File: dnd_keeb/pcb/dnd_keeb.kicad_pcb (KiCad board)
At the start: 2 copper layers, 60 x 100 mm, 23 parts, among them J1 Conn_01x11, SW1 SW_DIP_x01, SW2 SW_DIP_x01, SW3 SW_DIP_x01, SW4 SW_DIP_x01, SW5 SW_DIP_x01, SW6 SW_DIP_x01, SW7 SW_DIP_x01, SW8 SW_DIP_x01, SW9 SW_DIP_x01, U1 OLED_326

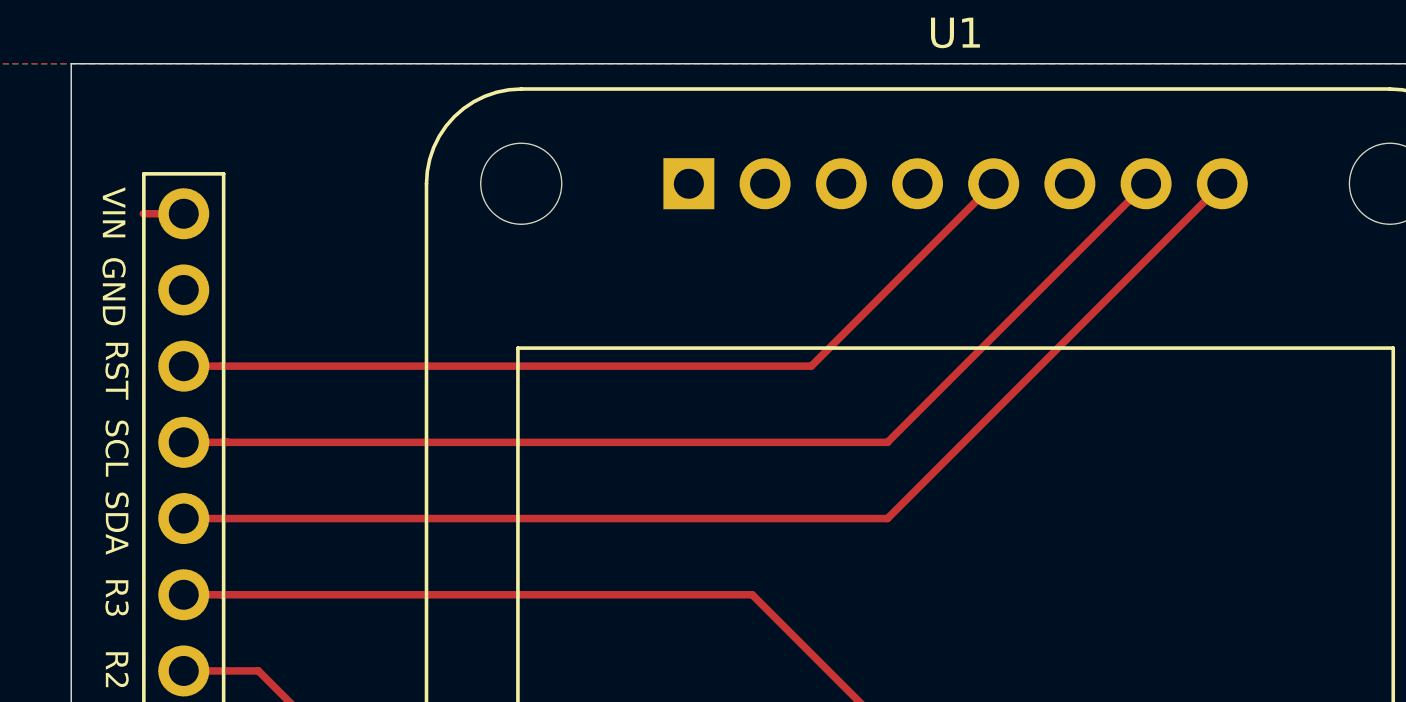
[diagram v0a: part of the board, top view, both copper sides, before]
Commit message: 🐛 [dnd_keeb] Fix pinout for OLED & update footprints + pcb
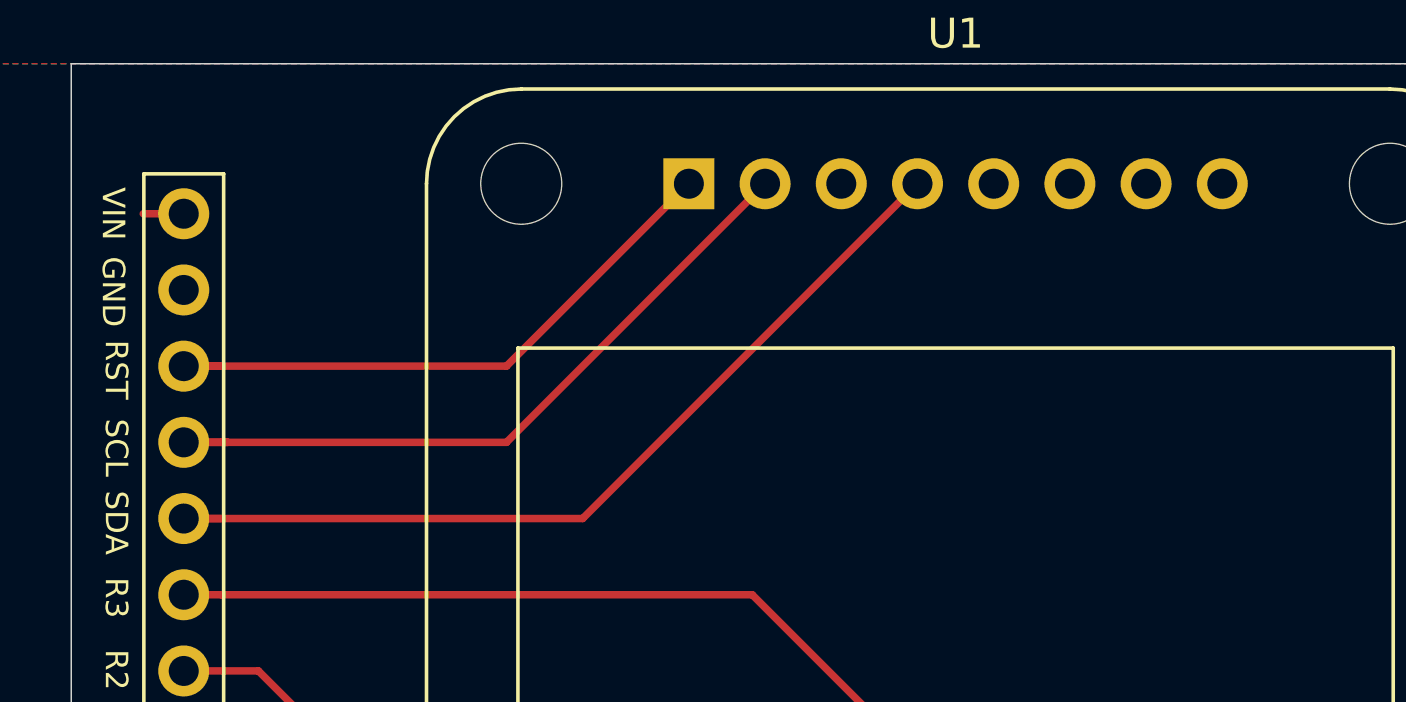
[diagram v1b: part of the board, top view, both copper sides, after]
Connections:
- J1 pad 7: SDA -> RST
- J1 pad 9: RST -> SDA
- U1 pad 1: GND -> SDA
- U1 pad 2: VIN -> SCL
- U1 pad 4: Net-(U1-Pad4) -> RST
- U1 pad 5: RST -> Net-(U1-Pad5)
- U1 pad 7: SCL -> VIN
- U1 pad 8: SDA -> GND
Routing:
- net SDA: track 39.2 -> 21.0 mm
- net SCL: track 35.9 -> 24.6 mm
- net RST: track 29.5 -> 30.3 mm

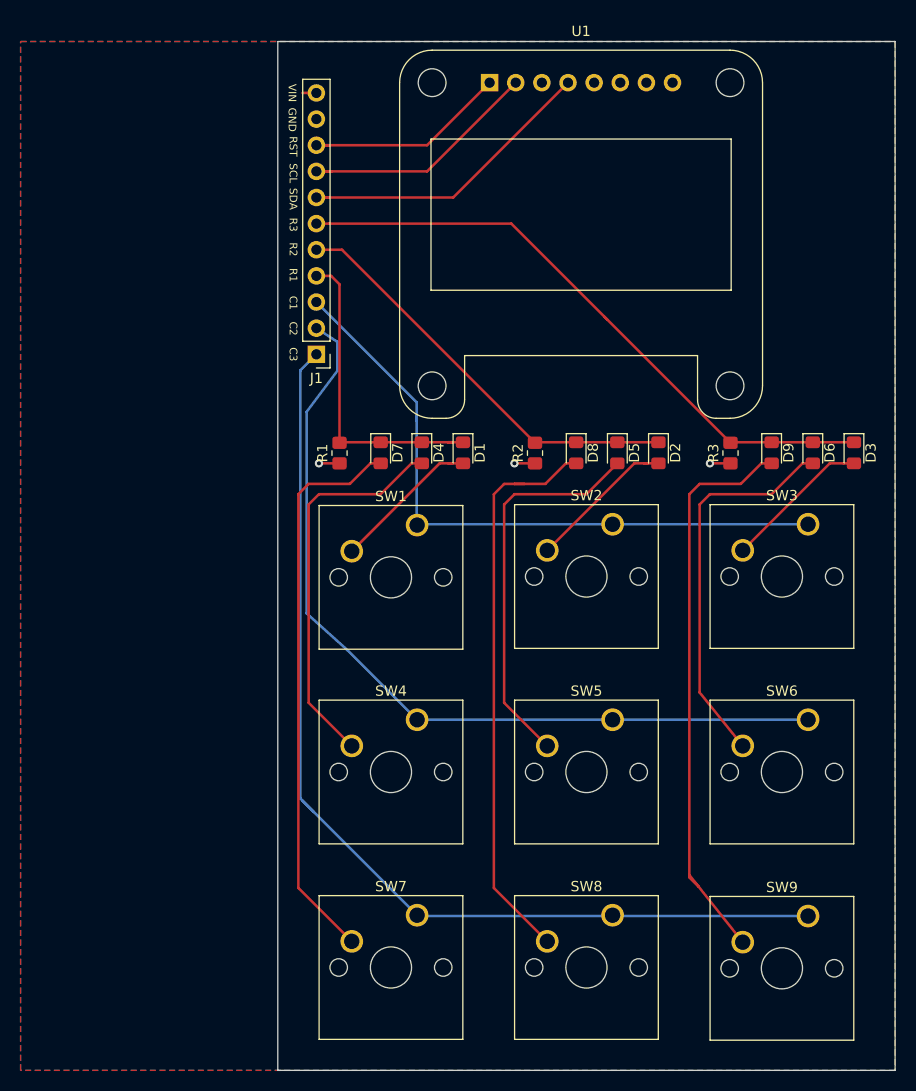
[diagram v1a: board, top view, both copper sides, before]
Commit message: ✨ [dnd_keeb] v0.2
- Added atmega4809 to board, routed row/cols + lcd to mcu
- Added ICSP + TX/RX pinout to program / debug
- Added USB micro for power
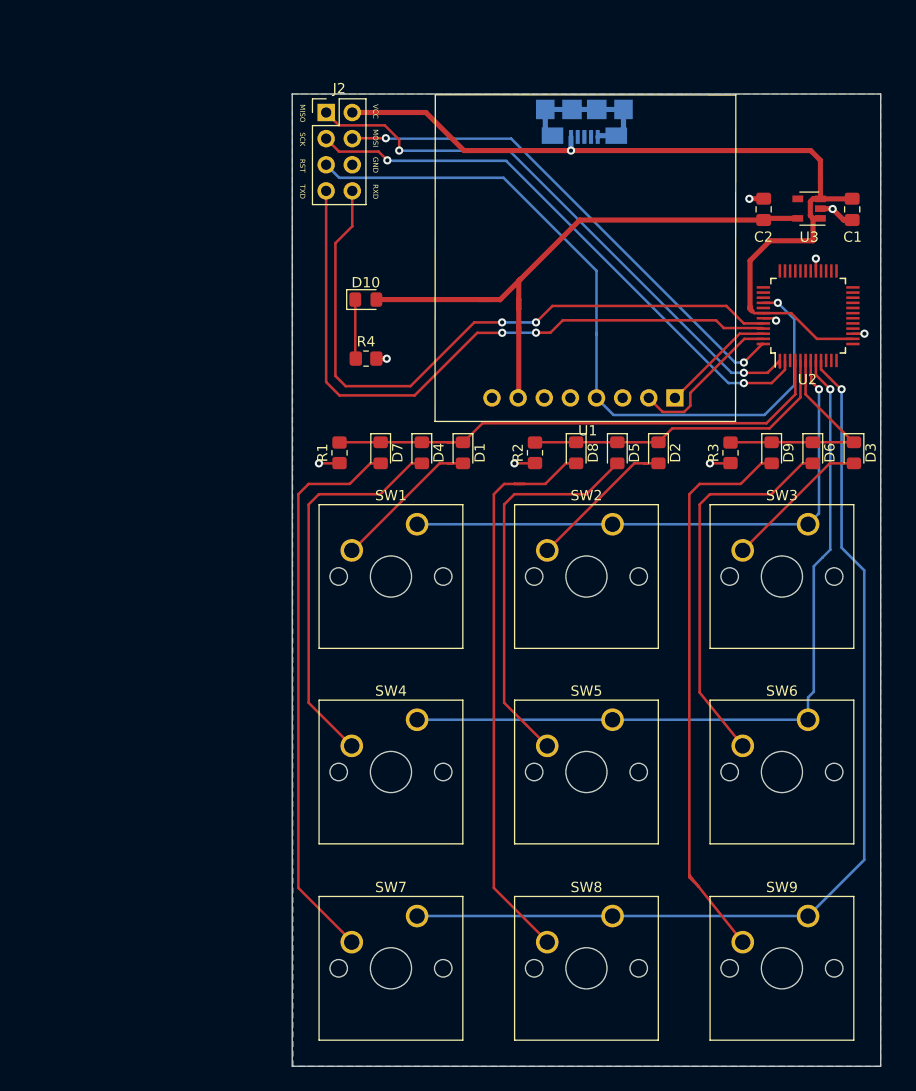
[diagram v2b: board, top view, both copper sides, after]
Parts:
- added C1: 1uF, Capacitor_SMD:C_0805_2012Metric_Pad1.18x1.45mm_HandSolder, F.Cu at (185.8, 36.3)
- added C2: 1uF, Capacitor_SMD:C_0805_2012Metric_Pad1.18x1.45mm_HandSolder, F.Cu at (177.2, 36.3)
- added D10: PWR, LED_SMD:LED_0805_2012Metric_Pad1.15x1.40mm_HandSolder, F.Cu at (138.6, 45.1)
- added J2: Conn_02x04_Odd_Even, Connector_PinHeader_2.54mm:PinHeader_2x04_P2.54mm_Vertical, F.Cu at (134.7, 26.9)
- added R4: 330, Resistor_SMD:R_0805_2012Metric_Pad1.20x1.40mm_HandSolder, F.Cu at (138.6, 50.8)
- added U2: ATmega4809-A, Package_QFP:TQFP-48_7x7mm_P0.5mm, F.Cu at (181.6, 46.6)
- added U3: AP2112K-3.3, Package_TO_SOT_SMD:SOT-23-5, F.Cu at (181.6, 36.2)
- J1: value Conn_01x11 -> USB-B Micro Receptacle 10118192-0002LF; footprint Connector_PinHeader_2.54mm:PinHeader_1x11_P2.54mm_Vertical -> dnd_keeb:AMPHENOL_10118192-0002LF; moved to B.Cu
- U1: footprint Display:Adafruit_SSD1306 -> dnd_keeb:Adafruit_326
- moved J1 33.5 mm to (159.8, 29.3), turned to 0 degrees
- moved U1 32.8 mm to (162.2, 54.7), turned to 180 degrees
- moved SW1 0.08 mm to (143.5, 66.9)
- moved SW7 0.08 mm to (143.5, 105.0)
- moved SW8 0.08 mm to (162.5, 105.0)
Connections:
- J1 pad 1: COL3 -> VCC
- J1 pad 2: COL2 -> Net-(J1-Pad2)
- J1 pad 3: COL1 -> Net-(J1-Pad3)
- J1 pad 4: ROW1 -> Net-(J1-Pad4)
- J1 pad 5: ROW2 -> GND
- U1 pad 7: VIN -> 3v3
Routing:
- net VCC: track 0.00 -> 84.1 mm, vias 0 -> 1
- net /RXD: track 0.00 -> 65.1 mm, vias 0 -> 2
- net /TXD: track 0.00 -> 64.6 mm, vias 0 -> 2
- net 3v3: track 0.00 -> 58.6 mm
- net MISO: track 0.00 -> 56.4 mm, vias 0 -> 2
- net SCK: track 0.00 -> 55.9 mm, vias 0 -> 2
- net MOSI: track 0.00 -> 50.1 mm, vias 0 -> 2
- net RST: track 30.3 -> 74.3 mm, vias 0 -> 1
- net ROW3: track 61.4 -> 21.9 mm
- net GND: track 6.00 -> 30.7 mm, vias 3 -> 9
- net ROW1: track 30.5 -> 50.0 mm
- net SDA: track 21.0 -> 11.2 mm
- net ROW2: track 41.0 -> 31.2 mm
- net COL1: track 64.2 -> 54.8 mm, vias 0 -> 1
- net SCL: track 24.6 -> 15.4 mm
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- removed copper zone on F.Cu, net VIN
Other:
- board size 60 x 100 mm -> 57.2 x 94.5 mm
- board text added: "D&D Keeb v0.2"
- board text added: "MISO"
- board text added: "MOSI"
- board text added: "RXD"
- board text added: "SCK"
- board text added: "TXD"
- board text added: "VCC"
- board text removed: "C1"
- board text removed: "C2"
- board text removed: "C3"
- board text removed: "D&D Keeb v0.1"
- board text removed: "R1"
- board text removed: "R2"
- board text removed: "R3"
- board text removed: "SCL"
- board text removed: "SDA"
- board text removed: "VIN"

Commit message: 🐛 Updating schematic so that UPDI is correctly broken out to a PIN
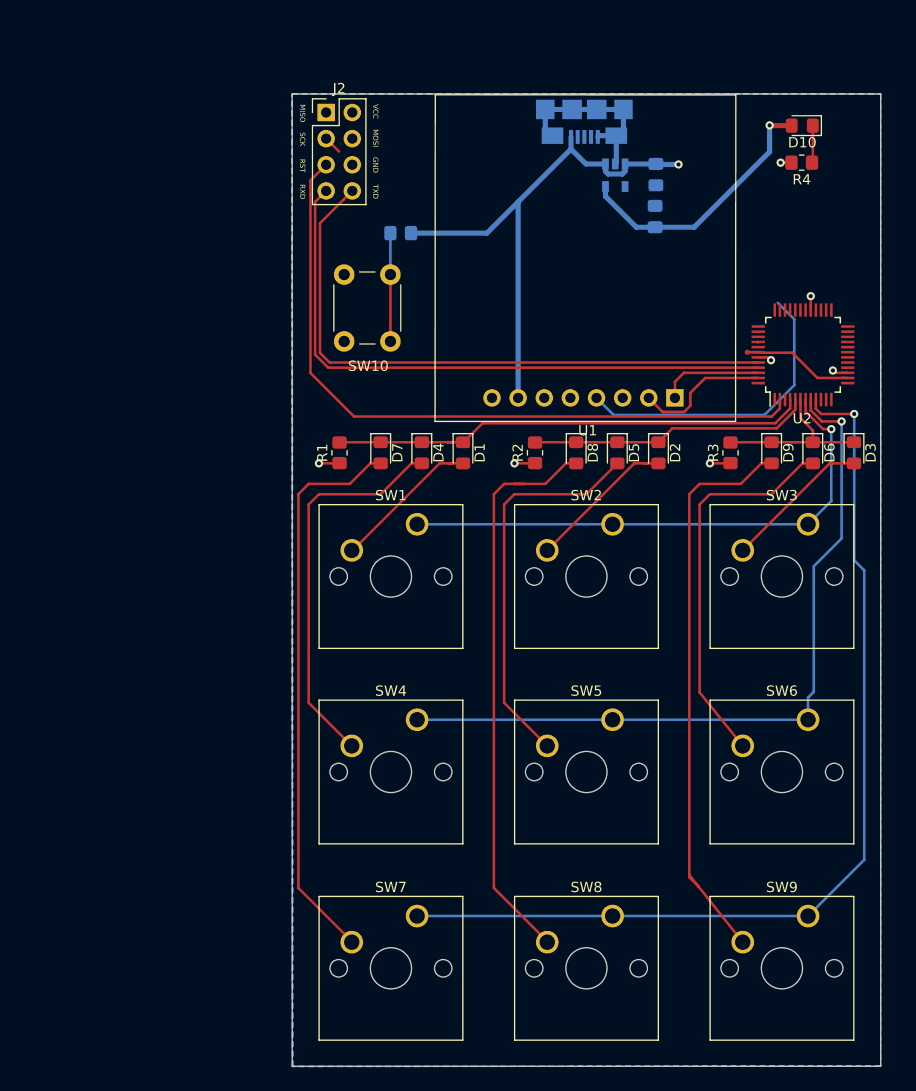
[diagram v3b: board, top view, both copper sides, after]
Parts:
- added R5: 330, Resistor_SMD:R_0805_2012Metric_Pad1.20x1.40mm_HandSolder, B.Cu at (141.9, 38.6)
- added SW10: SW_Push, Button_Switch_THT:SW_PUSH_6mm, F.Cu at (136.4, 49.1)
- C1, C2: moved to B.Cu
- U3: value AP2112K-3.3 -> AP7343-33W5-7; moved to B.Cu
- moved R4 46.4 mm to (180.9, 31.8), turned to 180 degrees
- moved D10 45.7 mm to (181.0, 28.2), turned to 180 degrees
- moved C1 19.4 mm to (166.8, 32.9)
- moved U3 19.1 mm to (162.8, 33.0), turned to 270 degrees
- moved C2 10.6 mm to (166.7, 37.0)
- moved U2 3.83 mm to (181.1, 50.5)
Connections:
- J2 pad 1: MISO -> MOSI
- J2 pad 3: SCK -> MISO
- J2 pad 4: MOSI -> UPDI
- J2 pad 5: RST -> SCK
- U1 pad 4: RST -> Net-(U1-Pad4)
- U1 pad 7: 3v3 -> VCC
- U2 pad 40: RST -> Net-(R5-Pad2)
- U2 pad 41: Net-(U2-Pad41) -> UPDI
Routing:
- net RST: track 74.3 -> 0.00 mm, vias 1 -> 0
- net MISO: track 56.4 -> 1.78 mm, vias 2 -> 0
- net MOSI: track 50.1 -> 0.00 mm, vias 2 -> 0
- net 3v3: track 58.6 -> 25.9 mm, vias 0 -> 1
- net Net-(U1-Pad4): track 0.00 -> 29.8 mm
- net VCC: track 84.1 -> 62.8 mm
- net SCK: track 55.9 -> 69.7 mm, vias 2 -> 0
- net Net-(R5-Pad2): track 0.00 -> 10.7 mm
- net ROW3: track 21.9 -> 16.7 mm
- net /RXD: track 65.1 -> 60.1 mm, vias 2 -> 0
- net /TXD: track 64.6 -> 60.0 mm, vias 2 -> 0
- net ROW2: track 31.2 -> 27.6 mm
- net ROW1: track 50.0 -> 46.5 mm
- net COL1: track 54.8 -> 52.6 mm
- net Net-(D10-Pad1): track 5.76 -> 3.63 mm
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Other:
- rule pad_to_mask_clearance: 0 -> 0.0508
